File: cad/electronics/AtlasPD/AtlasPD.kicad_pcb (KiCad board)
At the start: 4 copper layers, 57.1 x 50 mm, 47 parts, among them J201 USB_C_Receptacle_USB2.0, J202 Conn_01x04, J203 Conn_02x03_Odd_Even, J301 Conn_01x06, J302 Conn_01x06, SW201 SW_SPST, U201 CP2104, U202 ATmega328P-AU, U204 Arduino_MKR_Zero, U301 74LS08, U302 DRV8837C, U303 DRV8837C, U401 AMS1117-3.3, Y201 16MHz

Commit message: Small changes
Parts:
- added C206: 10uF, Capacitor_SMD:C_0402_1005Metric, F.Cu at (317.7, 114.0)
- added C207: 10u, Capacitor_SMD:C_0402_1005Metric, F.Cu at (326.4, 115.8)
- added C208: 10u, Capacitor_SMD:C_0402_1005Metric, F.Cu at (326.4, 113.8)
- added C209: 10n, Capacitor_SMD:C_0402_1005Metric, F.Cu at (326.4, 111.9)
- added C210: 10n, Capacitor_SMD:C_0402_1005Metric, F.Cu at (329.2, 111.9)
- added U203: AMS1117-3.3, Package_TO_SOT_SMD:SOT-223-3_TabPin2, F.Cu at (318.3, 102.9)
- C201, C202, C203, C204, C205: footprint Capacitor_SMD:C_0603_1608Metric -> Capacitor_SMD:C_0402_1005Metric
- D201, D202, D203, D204: footprint LED_SMD:LED_0603_1608Metric -> LED_SMD:LED_0402_1005Metric
- R202, R203, R204, R205, R206, R207, R208, R209: footprint Resistor_SMD:R_0603_1608Metric -> Resistor_SMD:R_0402_1005Metric
- moved R202 132.6 mm to (327.8, 99.8), turned to 0 degrees
- moved R203 127.7 mm to (324.6, 101.8), turned to 0 degrees
- moved C201 125.9 mm to (317.7, 112.0), turned to 0 degrees
- moved C202 124.4 mm to (324.6, 105.8), turned to 0 degrees
- moved C205 111.4 mm to (324.0, 108.0), turned to 0 degrees
- moved R208 109.9 mm to (314.8, 114.0), turned to 0 degrees
- moved C203 99.9 mm to (320.8, 110.0), turned to 0 degrees
- moved R209 96.6 mm to (321.1, 108.1), turned to 0 degrees
- moved C204 96.5 mm to (314.8, 116.0), turned to 0 degrees
- moved D201 4.55 mm to (225.3, 36.4)
- moved D204 4.37 mm to (225.3, 37.5)
- moved D203 4.24 mm to (225.3, 38.5)
- moved D202 4.19 mm to (225.3, 39.5)
- moved R204 3.46 mm to (223.4, 36.4)
- moved R207 3.22 mm to (223.4, 37.5)
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- renumbered U204 to U500
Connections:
- net /Sheet60A2E58A/IO13_SCK renamed /Motor Driver/~{SLEEP}
- U302 pad 5: /Motor Driver/OUT2 -> /Sheet60A2E58A/IO3
- U302 pad 6: /Motor Driver/OUT1 -> /Sheet60A2E58A/IO2
- U303 pad 1: +BATT -> unconnected-(U303-Pad1)
- U303 pad 5: /Motor Driver/OUT4 -> /Sheet60A2E58A/IO6
- U303 pad 6: /Motor Driver/OUT3 -> /Sheet60A2E58A/IO5
- U303 pad 8: VCC -> unconnected-(U303-Pad8)
- U500 pad 10: unconnected-(U204-Pad10) -> /Arduino MKR Zero/IN_2
- U500 pad 11: unconnected-(U204-Pad11) -> /Arduino MKR Zero/IN_3
- U500 pad 12: unconnected-(U204-Pad12) -> /Arduino MKR Zero/IN_4
- U500 pad 14: unconnected-(U204-Pad14) -> /Arduino MKR Zero/EN
- U500 pad 15: unconnected-(U204-Pad15) -> /Arduino MKR Zero/S1
- U500 pad 16: unconnected-(U204-Pad16) -> /Arduino MKR Zero/S2
- U500 pad 17: unconnected-(U204-Pad17) -> /Arduino MKR Zero/S3
- U500 pad 18: unconnected-(U204-Pad18) -> /Arduino MKR Zero/S4
- U500 pad 9: unconnected-(U204-Pad9) -> /Arduino MKR Zero/IN_1
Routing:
- net /Sheet60A2E58A/IO7: track 49.4 -> 4.76 mm
- net /Motor Driver/OUT2: track 34.8 -> 0.00 mm, vias 2 -> 0
- net /Motor Driver/OUT1: track 31.1 -> 0.00 mm, vias 2 -> 0
- net /Motor Driver/OUT3: track 26.9 -> 0.00 mm, vias 2 -> 0
- net /Sheet60A2E58A/IO4: track 29.2 -> 4.76 mm
- net /Motor Driver/OUT4: track 22.9 -> 0.00 mm, vias 2 -> 0
- net /Sheet60A2E58A/IO3: track 19.7 -> 34.8 mm, vias 0 -> 2
- net /Sheet60A2E58A/IO6: track 37.4 -> 22.9 mm, vias 0 -> 2
- net /Sheet60A2E58A/IO5: track 39.2 -> 26.9 mm, vias 0 -> 2
- net /Sheet60A2E58A/IO2: track 20.9 -> 31.1 mm, vias 0 -> 2
- net Net-(R205-Pad1): track 6.03 -> 0.00 mm
- net Net-(R206-Pad1): track 5.59 -> 0.00 mm
- net Net-(J201-PadA5): track 3.28 -> 0.00 mm
- net Net-(J201-PadB5): track 2.86 -> 0.00 mm
- net /Sheet60A2E58A/DTR: track 27.4 -> 25.0 mm
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- removed copper zone on F.Cu, net +5V

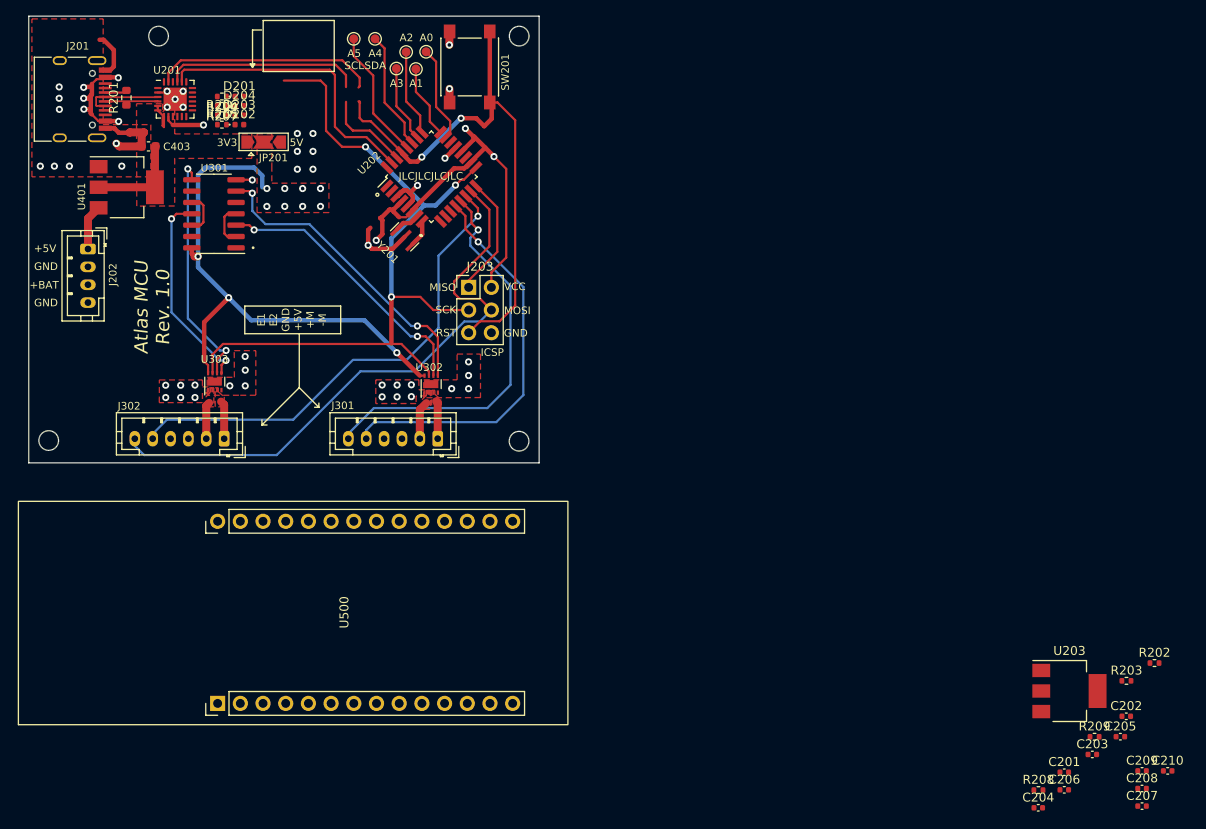
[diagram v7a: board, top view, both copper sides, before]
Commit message: Added Photos, Started Fixing Bugs for a potential revision to stm-cerberus
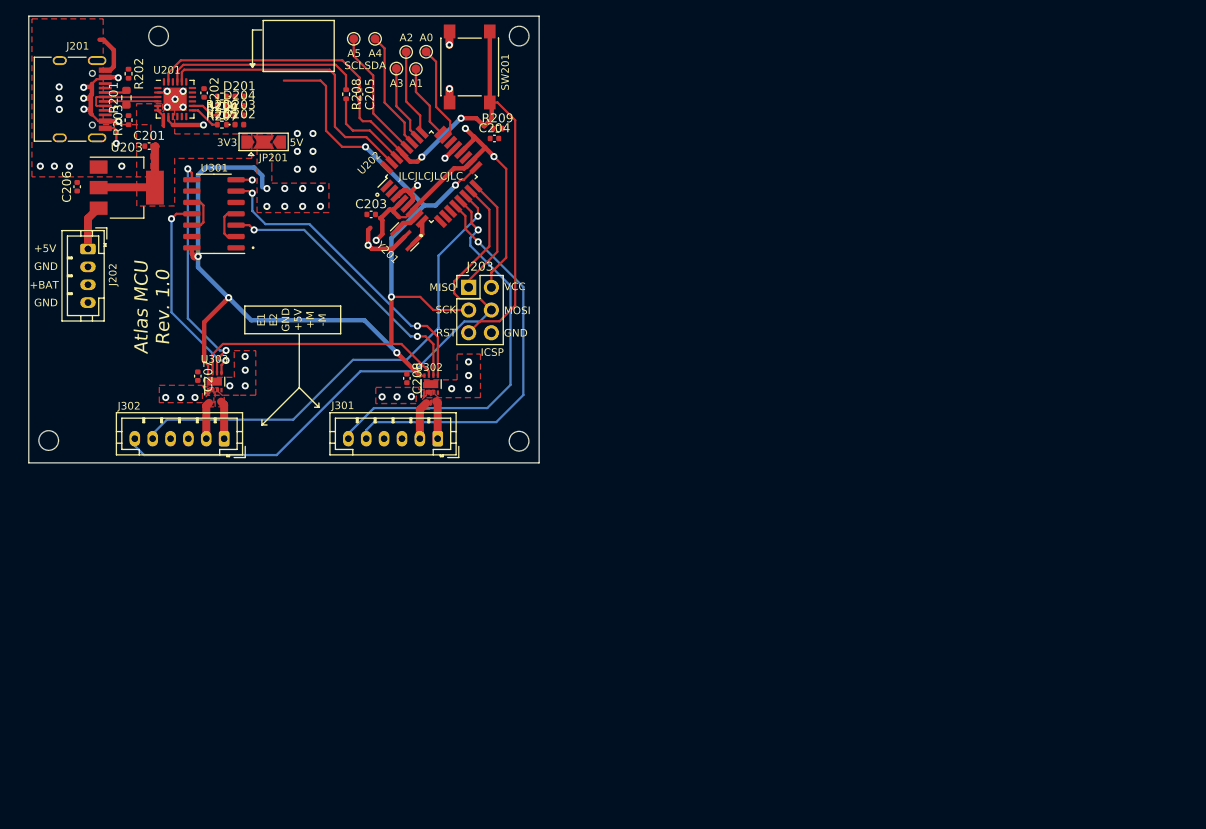
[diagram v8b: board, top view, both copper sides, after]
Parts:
- removed C209, C210: 10n, Capacitor_SMD:C_0402_1005Metric
- removed C403: 10uF, Capacitor_SMD:C_0603_1608Metric
- removed U401: AMS1117-3.3, Package_TO_SOT_SMD:SOT-223-3_TabPin2
- removed U500: Arduino_MKR_Zero, SamacSys_Parts:Arduino MKR Zero
- moved R202 132.4 mm to (212.9, 33.9), turned to -90 degrees
- moved C206 129.5 mm to (207.2, 46.5), turned to 90 degrees
- moved R203 128.1 mm to (212.9, 39.0), turned to 90 degrees
- moved C202 124.6 mm to (221.4, 36.0), turned to -90 degrees
- moved C201 124.1 mm to (215.2, 42.0)
- moved U203 119.6 mm to (212.8, 46.6)
- moved C207 116.1 mm to (220.7, 67.7), turned to -90 degrees
- moved C205 111.4 mm to (238.8, 36.1), turned to -90 degrees
- moved R208 109.9 mm to (237.3, 36.1), turned to -90 degrees
- moved C203 100.8 mm to (240.1, 49.6)
- moved C204 96.5 mm to (253.9, 41.1)
- moved R209 95.4 mm to (254.2, 40.0)
- moved C208 94.2 mm to (244.1, 68.0), turned to -90 degrees
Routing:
- net GND: track 33.8 -> 27.3 mm
- net Net-(R205-Pad1): track 0.00 -> 3.45 mm
- net Net-(R206-Pad1): track 0.00 -> 3.23 mm
- net +BATT: vias 12 -> 6
